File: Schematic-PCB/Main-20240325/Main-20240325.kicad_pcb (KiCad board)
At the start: 2 copper layers, 115 x 115 mm, 108 parts, among them J1 Conn_01x10_Pin, J2 Conn_01x03_Pin, J3 Conn_01x15_Pin, J4 Conn_02x05_Odd_Even, J5 Conn_01x04_Pin, U1 DEV-16771, U10 TSSP58038, U11 TSSP58038, U12 TSSP58038, U13 TSSP58038, U14 TSSP58038, U15 TSSP58038, U16 TSSP58038, U17 TSSP58038, U18 TSSP58038, U19 TSSP58038, U4 TSSP58038, U5 TSSP58038, U6 TSSP58038, U7 TSSP58038, U8 TSSP58038, U9 TSSP58038

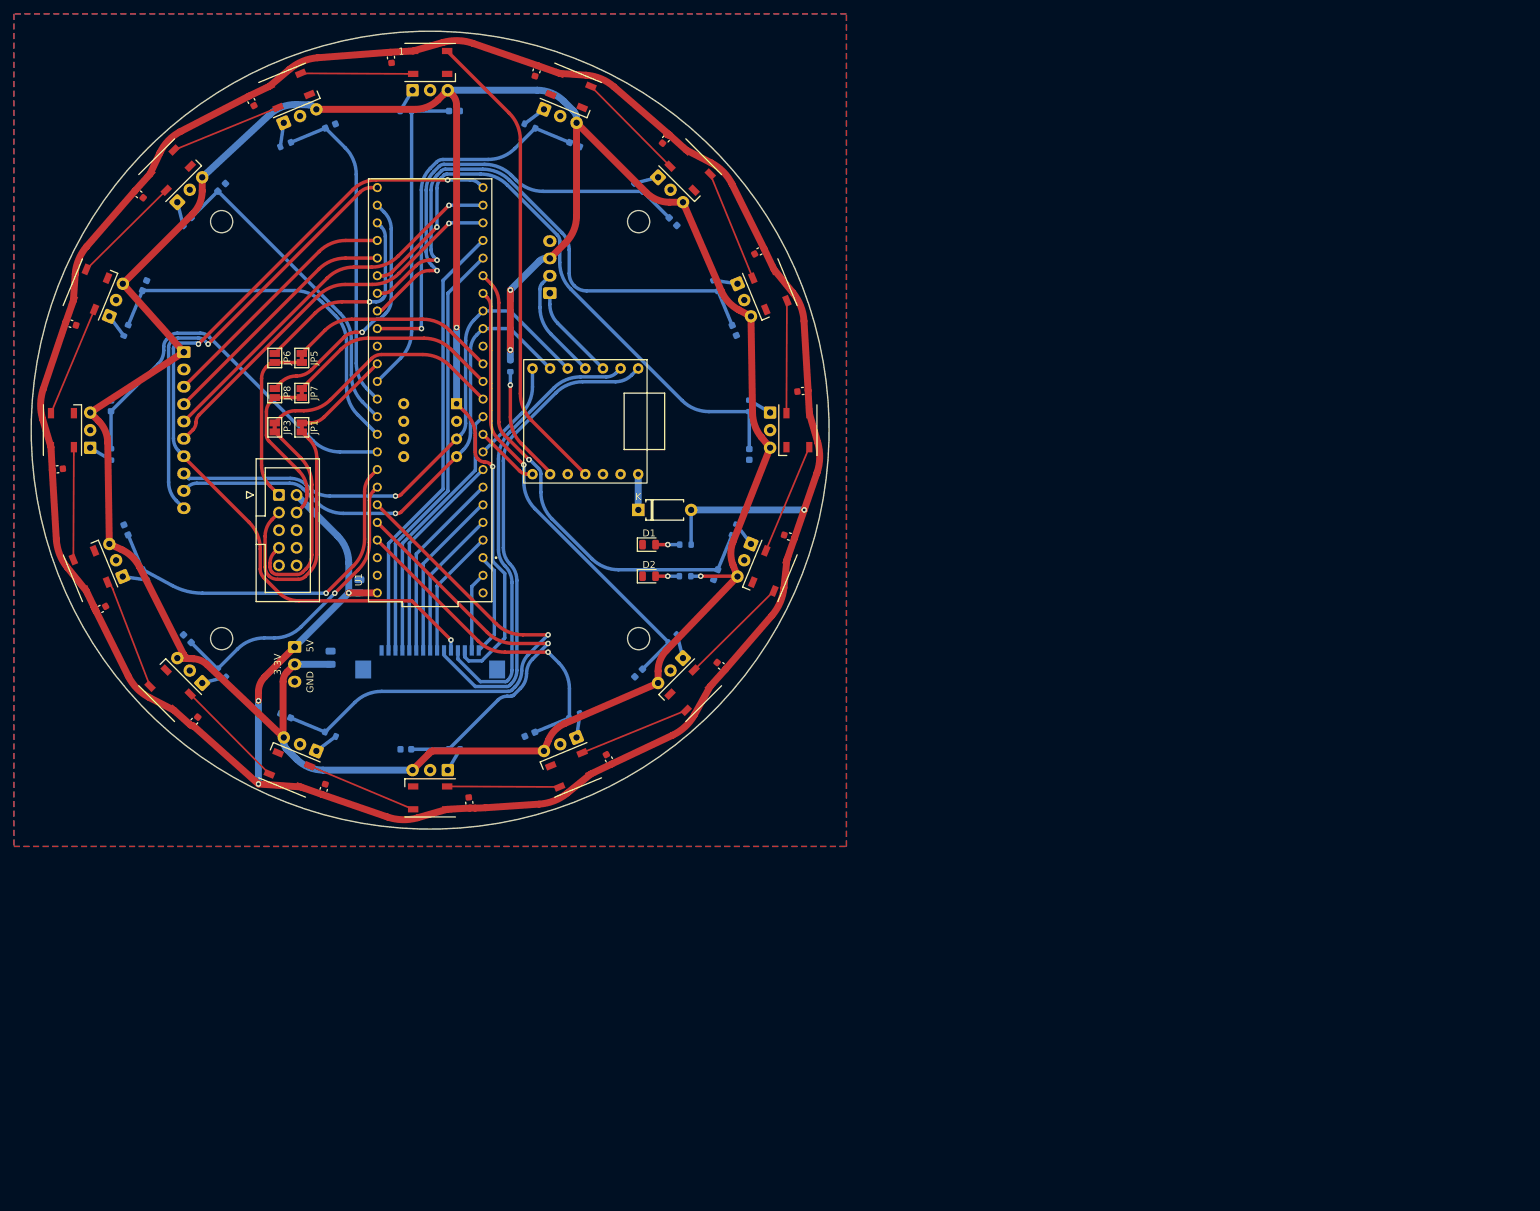
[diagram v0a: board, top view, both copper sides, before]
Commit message: UI基板を修正/MD基板を修正/メイン基板を作り直し （ver.002）
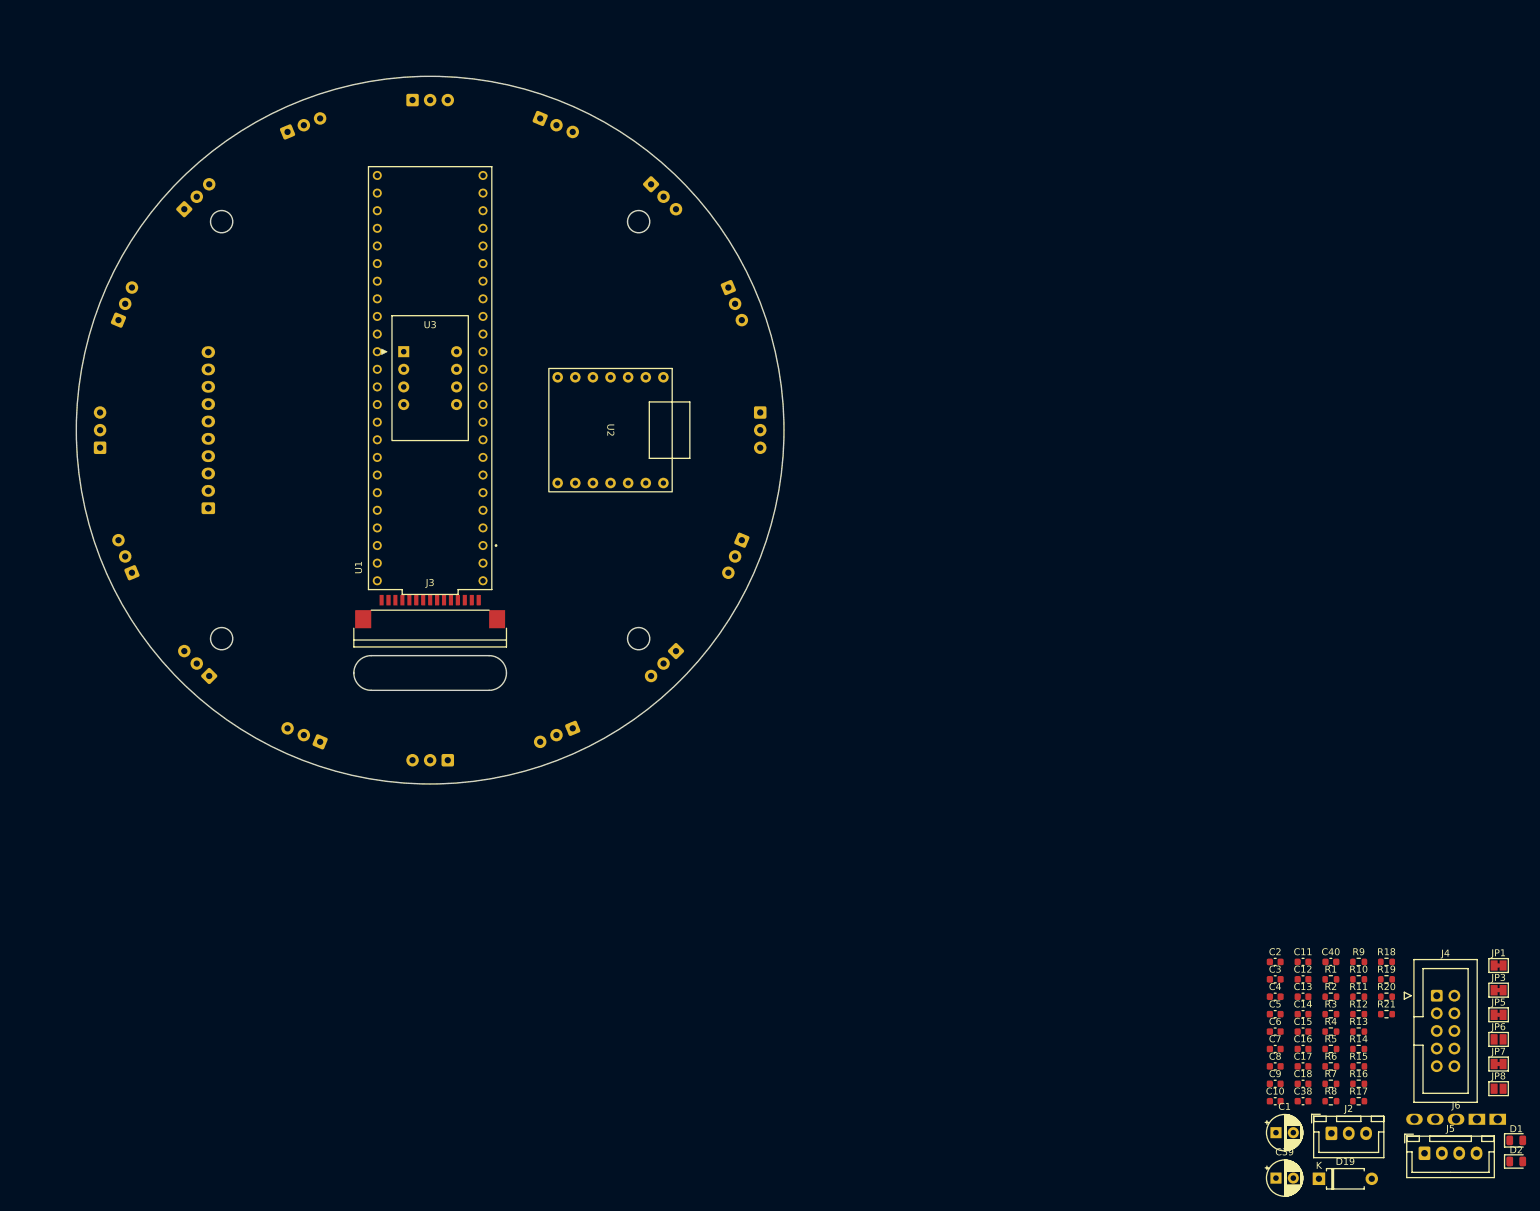
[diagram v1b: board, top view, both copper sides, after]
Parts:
- removed C19, C20, C21, C22, C23, C24, C25, C26, C27, C28, C29, C30, C31, C32, C33, C34: 0.1uF, Capacitor_SMD:C_0603_1608Metric
- removed D10, D11, D12, D13, D14, D15, D16, D17, D18, D3, D4, D5, D6, D7, D8, D9: WS2812B, LED_SMD:LED_WS2812B_PLCC4_5.0x5.0mm_P3.2mm
- removed REF** (x4): MountingHole_3.2mm_M3, MountingHole:MountingHole_3.2mm_M3
- added C38: 0.1uF, Capacitor_SMD:C_0603_1608Metric, F.Cu at (125.8, 96.7)
- added C39: 100uF, Capacitor_THT:CP_Radial_D5.0mm_P2.50mm, F.Cu at (121.9, 107.8)
- added C40: 0.1uF, Capacitor_SMD:C_0603_1608Metric, F.Cu at (129.8, 76.6)
- added J6: Conn_01x05_Pin, @2024TOINIOT2-Main:Connector, F.Cu at (147.9, 99.3)
- C1: value C -> 100uF; footprint Capacitor_SMD:C_0805_2012Metric -> Capacitor_THT:CP_Radial_D5.0mm_P2.50mm; moved to F.Cu
- C10, C11, C12, C13, C14, C15, C16, C17, C18, C3, C4, C5, C6, C7, C8, C9, J2, J3, J5, R1, R10, R11, R12, R13, R14, R15, R16, R17, R18, R19, R2, R20, R21, R3, R4, R5, R6, R7, R8, R9, U3: moved to F.Cu
- C2: value C -> 0.1uF; footprint Capacitor_SMD:C_0805_2012Metric -> Capacitor_SMD:C_0603_1608Metric; moved to F.Cu
- moved R8 207.9 mm to (129.8, 96.7), turned to 0 degrees
- moved JP8 202.9 mm to (154.0, 94.9), turned to 0 degrees
- moved R7 202.5 mm to (129.8, 94.2), turned to 0 degrees
- moved JP6 201.9 mm to (154.0, 87.8), turned to 0 degrees
- moved R9 199.6 mm to (133.8, 76.6), turned to 0 degrees
- moved JP7 197.8 mm to (154.0, 91.4), turned to 0 degrees
- moved JP5 196.8 mm to (154.0, 84.3), turned to 0 degrees
- moved C6 195.2 mm to (121.8, 86.7), turned to 0 degrees
- moved R10 195.1 mm to (133.8, 79.2), turned to 0 degrees
- moved JP3 194.2 mm to (154.0, 80.7), turned to 0 degrees
- moved C5 193.0 mm to (121.8, 84.2), turned to 0 degrees
- moved C7 191.7 mm to (121.8, 89.2), turned to 0 degrees
- moved R6 191.7 mm to (129.8, 91.7)
- moved JP1 189.1 mm to (154.0, 77.2), turned to 0 degrees
- moved R11 185.3 mm to (133.8, 81.7), turned to 0 degrees
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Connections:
- C2 pad 1: +3.3V -> +5V
- J2 pad 1: +5V -> 5.0V
- J2 pad 2: +3.3V -> 3.3V
- J3 pad 1: Line-RX -> GND
- J3 pad 10: EN-3 -> ball01k
- J3 pad 11: PH-2 -> KickerSignal
- J3 pad 12: EN-2 -> ball02k
- J3 pad 13: PH-1 -> +3.3V
- J3 pad 14: EN-1 -> Line-TX
- J3 pad 15: GND -> Line-RX
- J3 pad 2: Line-TX -> EN-1
- J3 pad 3: +3.3V -> PH-1
- J3 pad 4: ball02k -> EN-2
- J3 pad 5: KickerSignal -> PH-2
- J3 pad 6: ball01k -> EN-3
- J3 pad 7: PH-4 -> PH-3
- J3 pad 9: PH-3 -> PH-4
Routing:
- net +3.3V: track 485.6 -> 0.00 mm, vias 5 -> 0
- net +5V: track 431.6 -> 0.00 mm, vias 4 -> 0
- net KickerSignal: track 125.0 -> 0.00 mm, vias 3 -> 0
- net ball13: track 85.4 -> 0.00 mm, vias 1 -> 0
- net ball14: track 79.4 -> 0.00 mm, vias 1 -> 0
- net SDA: track 79.0 -> 0.00 mm, vias 1 -> 0
- net ball08: track 76.4 -> 0.00 mm, vias 1 -> 0
- net SCL: track 76.2 -> 0.00 mm, vias 1 -> 0
- net ball12: track 70.7 -> 0.00 mm, vias 1 -> 0
- net ball01k: track 70.1 -> 0.00 mm
- net NeoPixel_PWM: track 68.7 -> 0.00 mm
- net ball11: track 66.3 -> 0.00 mm, vias 1 -> 0
- net ball02k: track 66.1 -> 0.00 mm
- net EN-1: track 64.7 -> 0.00 mm
- net BUZZER: track 64.2 -> 0.00 mm, vias 1 -> 0
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- removed copper zone on B.Cu, net GND
- removed copper zone on F.Cu, net GND
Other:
- board size 115 x 115 mm -> 102 x 102 mm
- board text removed: "3.3V"
- board text removed: "5V"
- board text removed: "GND"

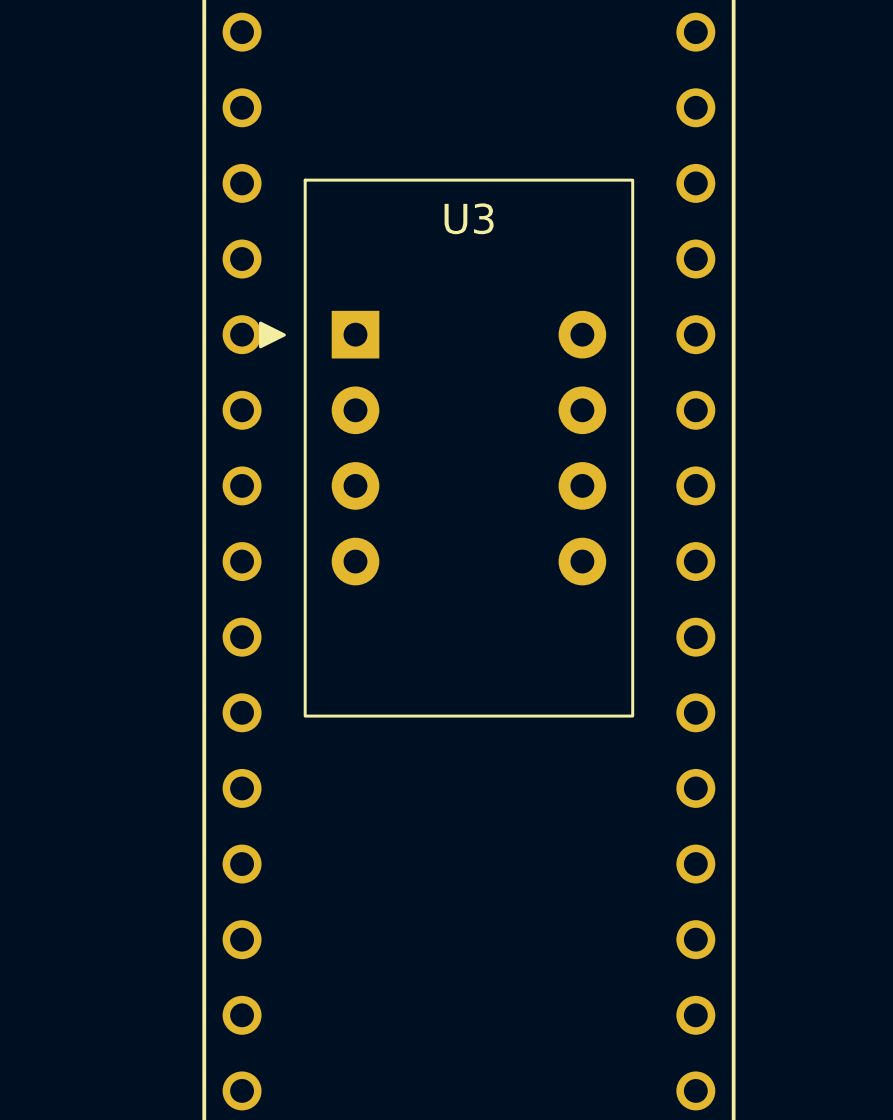
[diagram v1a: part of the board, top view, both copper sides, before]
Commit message: BNO055が基板の中央に来るように配置した
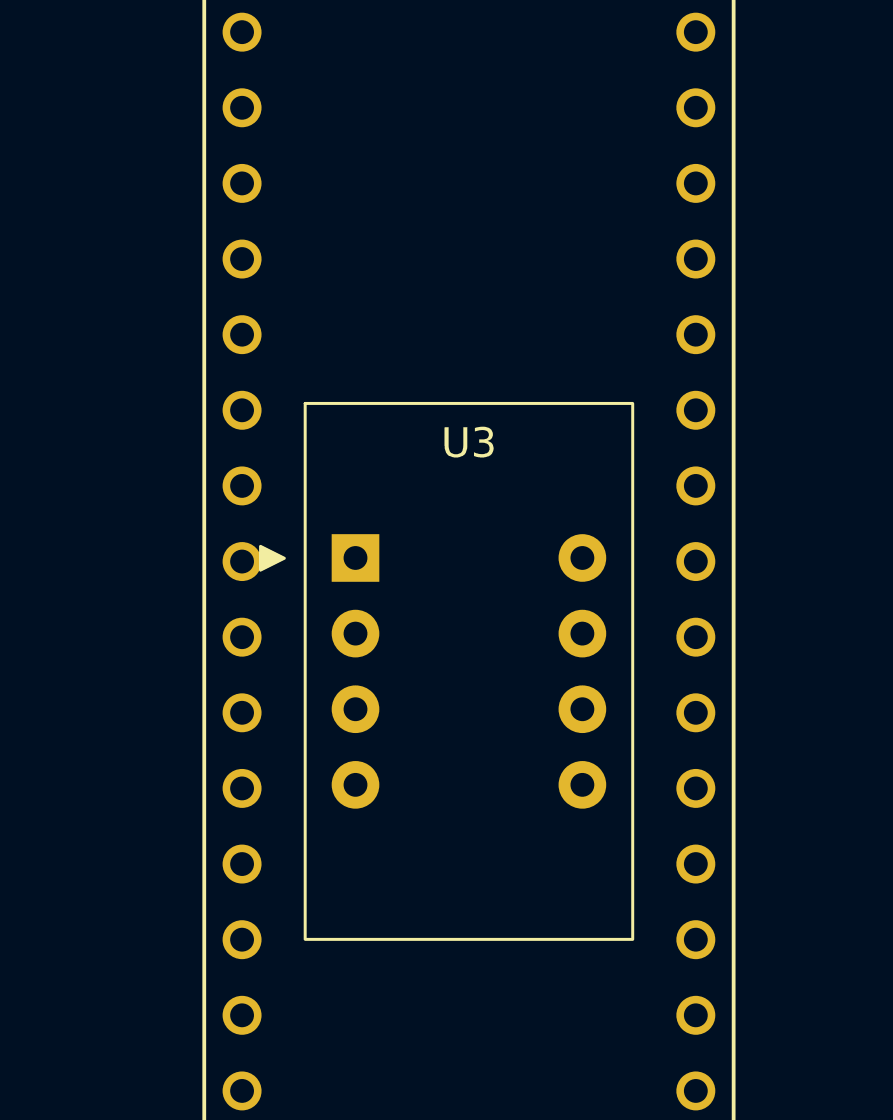
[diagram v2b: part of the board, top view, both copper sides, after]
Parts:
- moved U3 7.50 mm to (0.00, 0.00)
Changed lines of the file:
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@@
 	(footprint "@2024TOINIOT2-Main:BNO055"
 		(layer "F.Cu")
-		(at 0 -7.5)
+		(at 0 0)
 		(property "Reference" "U3"
 			(at 0 -7.665 0)

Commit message: メイン基板の部品を大雑把に配置&配線した
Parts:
- U3: moved to B.Cu
- moved JP8 211.4 mm to (-22.2, -21.8), turned to -90 degrees
- moved JP3 206.7 mm to (-22.2, -27.2), turned to -90 degrees
- moved R8 206.6 mm to (-34.3, -28.8), turned to 50 degrees
- moved JP7 205.7 mm to (-17.8, -21.8), turned to -90 degrees
- moved JP6 204.7 mm to (-22.2, -16.4), turned to -90 degrees
- moved R7 201.4 mm to (-20.7, -39.7), turned to 27.5 degrees
- moved JP1 201.0 mm to (-17.8, -27.2), turned to -90 degrees
- moved JP5 199.1 mm to (-17.8, -16.4), turned to -90 degrees
- moved R9 198.2 mm to (-42.7, -13.5), turned to 72.5 degrees
- moved C6 194.0 mm to (-39.3, -21.4), turned to 61.5 degrees
- moved R10 193.6 mm to (-44.6, 3.90), turned to 95 degrees
- moved C5 191.4 mm to (-28.2, -34.8), turned to 39 degrees
- moved C7 191.0 mm to (-44.5, -4.68), turned to 84 degrees
- moved R6 190.9 mm to (-3.90, -44.6), turned to 5 degrees
- moved J4 187.6 mm to (-21.3, -5.10)
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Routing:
- net +3.3V: track 0.00 -> 329.8 mm
- net SW-TAC-3: track 0.00 -> 86.8 mm
- net ball11: track 0.00 -> 83.6 mm
- net SW-TAC-4: track 0.00 -> 74.7 mm
- net ball13: track 0.00 -> 69.9 mm, vias 0 -> 1
- net ball12: track 0.00 -> 68.3 mm
- net ball03: track 0.00 -> 67.3 mm, vias 0 -> 1
- net ball10: track 0.00 -> 65.2 mm
- net KickerSignal: track 0.00 -> 63.5 mm
- net EN-1: track 0.00 -> 59.2 mm
- net ball02: track 0.00 -> 56.5 mm, vias 0 -> 1
- net PH-1: track 0.00 -> 56.3 mm
- net ball14: track 0.00 -> 56.2 mm, vias 0 -> 1
- net ball05: track 0.00 -> 53.8 mm
- net ball15: track 0.00 -> 53.6 mm, vias 0 -> 1
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
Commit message: 配線を進めた
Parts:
- moved R3 15.6 mm to (-28.9, 6.75), turned to 180 degrees
- moved R4 9.51 mm to (-27.2, 3.25)
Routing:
- net SDA: track 46.5 -> 91.2 mm
- net SCL: track 36.9 -> 79.3 mm
- net MISO: track 0.70 -> 35.2 mm, vias 0 -> 1
- net MOSI: track 11.5 -> 37.6 mm, vias 0 -> 1
- net Cam_SS: track 0.00 -> 19.2 mm
- net SW-TAC-4: track 74.7 -> 62.3 mm
- net +3.3V: track 329.8 -> 341.2 mm, vias 0 -> 1
- net SW-TAC-3: track 86.8 -> 80.6 mm
- net ball02: track 56.5 -> 50.4 mm
- net Cam-TX: track 19.5 -> 23.6 mm
- net Cam-MOSI_TX: track 11.8 -> 9.00 mm
- net KickerSignal: track 63.5 -> 61.5 mm
- net SCK: track 22.2 -> 24.1 mm
- net ball03: track 67.3 -> 65.7 mm
- net BUZZER: track 38.1 -> 39.3 mm
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
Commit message: 配線進めた
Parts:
- added U20: 74AHC1G32, Package_TO_SOT_SMD:SOT-23-5_HandSoldering, B.Cu at (3.95, 20.4)
- moved C40 4.40 mm to (-3.04, 7.50), turned to 0 degrees
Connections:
- J1 pad 7: KickerSignal -> KickerSignal-UI
- U1 pad 32: KickerSignal -> KickerSignal-Main
- U1 pad 36: SW-TAC-1 -> SW-TAC-2
- U1 pad 37: SW-TAC-2 -> SW-TAC-1
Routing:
- net ball01k: track 0.00 -> 67.0 mm
- net KickerSignal-Main: track 0.00 -> 58.0 mm, vias 0 -> 1
- net ball02k: track 0.00 -> 54.2 mm
- net KickerSignal: track 61.5 -> 7.34 mm, vias 0 -> 1
- net KickerSignal-UI: track 0.00 -> 52.8 mm, vias 0 -> 1
- net SW-TAC-1: track 0.00 -> 52.6 mm
- net SW-TAC-2: track 0.00 -> 51.2 mm
- net Cam_SS: track 19.2 -> 55.6 mm, vias 0 -> 1
- net Cam-MOSI_TX: track 9.00 -> 28.3 mm, vias 1 -> 0
- net +3.3V: track 341.2 -> 348.4 mm, vias 1 -> 2
- net SW-TAC-3: track 80.6 -> 74.1 mm
- net SCK: track 24.1 -> 21.3 mm
- net ball03: track 65.7 -> 63.1 mm
- net MOSI: track 37.6 -> 36.7 mm
- net Cam-MISO_RX: vias 0 -> 1
- added copper zone on B.Cu, net GND
- added copper zone on F.Cu, net GND
